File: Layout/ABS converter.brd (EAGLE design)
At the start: 91.1 x 50.8 mm, 31 parts, among them Q1 600mA/40V, Q2 600mA/40V, U2 LM358, U3 MAX9921AUB+, U4 LM358

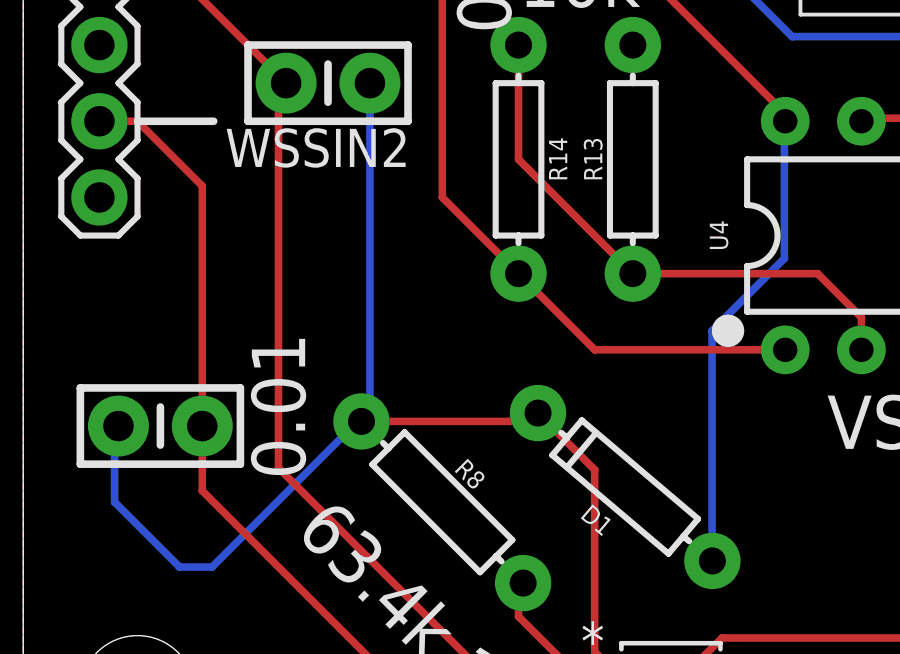
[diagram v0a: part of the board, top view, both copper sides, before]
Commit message: Added input filter cap to Max9921
This should have been in there from the get-go. It will hold the max up during momentary brownouts.
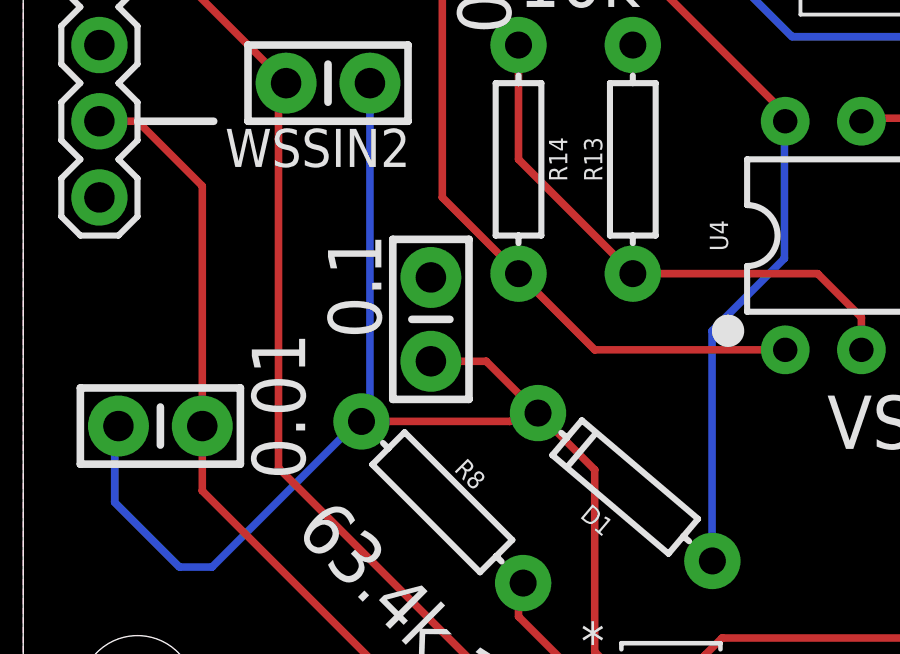
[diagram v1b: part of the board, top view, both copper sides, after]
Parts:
- added C7: 0.1uF, SparkFun-Capacitors:CAP-PTH-SMALL-KIT
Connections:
- net GND: now also C7.2
- net N$14: now also C7.1
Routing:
- net N$14: track 40.3 -> 44.6 mm
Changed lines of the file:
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@@
 <?xml version="1.0" encoding="utf-8"?>
 <!DOCTYPE eagle SYSTEM "eagle.dtd">
-<eagle version="9.4.2">
+<eagle version="9.6.0">
 <drawing>
 <settings>
@@
 <text x="9.017" y="9.144" size="1.778" layer="21" rot="R315">63.4k 1%</text>
 <text x="63.881" y="9.906" size="1.778" layer="21">Teensy 3.2</text>
+<text x="11.938" y="15.621" size="1.778" layer="21" rot="R90">0.1</text>
 </plain>
 <attributes>
@@
 <attribute name="VALUE" x="15.494" y="21.59" size="0.6096" layer="27" font="vector" ratio="20" rot="R270" align="top-center"/>
 </element>
+<element name="C7" library="SparkFun-Capacitors" package="CAP-PTH-SMALL-KIT" value="0.1uF" x="13.589" y="16.256" smashed="yes" rot="R90">
+<attribute name="PROD_ID" value="CAP-08370" x="13.589" y="16.256" size="1.778" layer="27" rot="R90" display="off"/>
+</element>
 </elements>
 <signals>
@@
 <vertex x="91.44" y="50.8"/>
 </polygon>
+<contactref element="C7" pad="2"/>
+<wire x1="86.233" y1="19.05" x2="85.09" y2="23.368" width="0" layer="19" extent="1-1"/>
+<wire x1="75.311" y1="31.877" x2="85.09" y2="23.368" width="0" layer="19" extent="1-1"/>
+<wire x1="67.31" y1="31.75" x2="75.311" y2="31.877" width="0" layer="19" extent="1-1"/>
+<wire x1="57.15" y1="25.4" x2="67.31" y2="31.75" width="0" layer="19" extent="1-1"/>
+<wire x1="51.07" y1="33.96" x2="57.15" y2="25.4" width="0" layer="19" extent="1-1"/>
+<wire x1="55.88" y1="44.45" x2="51.07" y2="33.96" width="0" layer="19" extent="1-1"/>
+<wire x1="40.37" y1="24.46" x2="51.07" y2="33.96" width="0" layer="19" extent="1-1"/>
+<wire x1="33.02" y1="15.24" x2="40.37" y2="24.46" width="0" layer="19" extent="1-1"/>
+<wire x1="20.32" y1="25.4" x2="33.02" y2="15.24" width="0" layer="19" extent="1-1"/>
+<wire x1="17.78" y1="30.353" x2="20.32" y2="25.4" width="0" layer="19" extent="1-1"/>
+<wire x1="23.86" y1="32.08" x2="17.78" y2="30.353" width="0" layer="19" extent="1-1"/>
+<wire x1="17.78" y1="37.973" x2="17.78" y2="30.353" width="0" layer="19" extent="1-1"/>
+<wire x1="17.78" y1="45.593" x2="17.78" y2="37.973" width="0" layer="19" extent="1-1"/>
+<wire x1="34.56" y1="41.58" x2="23.86" y2="32.08" width="0" layer="19" extent="1-1"/>
+<wire x1="2.54" y1="45.72" x2="17.78" y2="45.593" width="0" layer="19" extent="1-1"/>
+<wire x1="2.54" y1="40.64" x2="2.54" y2="45.72" width="0" layer="19" extent="1-1"/>
+<wire x1="2.54" y1="35.56" x2="2.54" y2="40.64" width="0" layer="19" extent="1-1"/>
+<wire x1="2.54" y1="30.48" x2="2.54" y2="35.56" width="0" layer="19" extent="1-1"/>
+<wire x1="2.54" y1="25.4" x2="2.54" y2="30.48" width="0" layer="19" extent="1-1"/>
+<wire x1="2.54" y1="20.32" x2="2.54" y2="25.4" width="0" layer="19" extent="1-1"/>
+<wire x1="19.4183" y1="2.81" x2="33.02" y2="15.24" width="0" layer="19" extent="1-1"/>
+<wire x1="13.589" y1="17.653" x2="19.4183" y2="2.81" width="0" layer="19" extent="1-1"/>
 </signal>
 <signal name="N$6">
@@
 <wire x1="3.048" y1="12.573" x2="3.175" y2="12.7" width="0.254" layer="16"/>
 <wire x1="19.4183" y1="4.81" x2="19.05" y2="5.1783" width="0.254" layer="1"/>
-<wire x1="19.05" y1="11.2425" x2="17.16023125" y2="13.13226875" width="0.254" layer="1"/>
+<wire x1="19.05" y1="11.2425" x2="17.68625" y2="12.60625" width="0.254" layer="1"/>
+<wire x1="17.68625" y1="12.60625" x2="17.16023125" y2="13.13226875" width="0.254" layer="1"/>
 <wire x1="19.05" y1="5.1783" x2="19.05" y2="11.2425" width="0.254" layer="1"/>
+<contactref element="C7" pad="1"/>
+<wire x1="13.589" y1="14.859" x2="15.4335" y2="14.859" width="0.254" layer="1"/>
+<wire x1="15.4335" y1="14.859" x2="17.16023125" y2="13.13226875" width="0.254" layer="1"/>
 </signal>
 <signal name="N$15">
